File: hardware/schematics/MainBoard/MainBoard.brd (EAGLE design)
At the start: 85.1 x 107.6 mm, 16 parts, among them J1 T2M-105-01-X-D-TH-WT

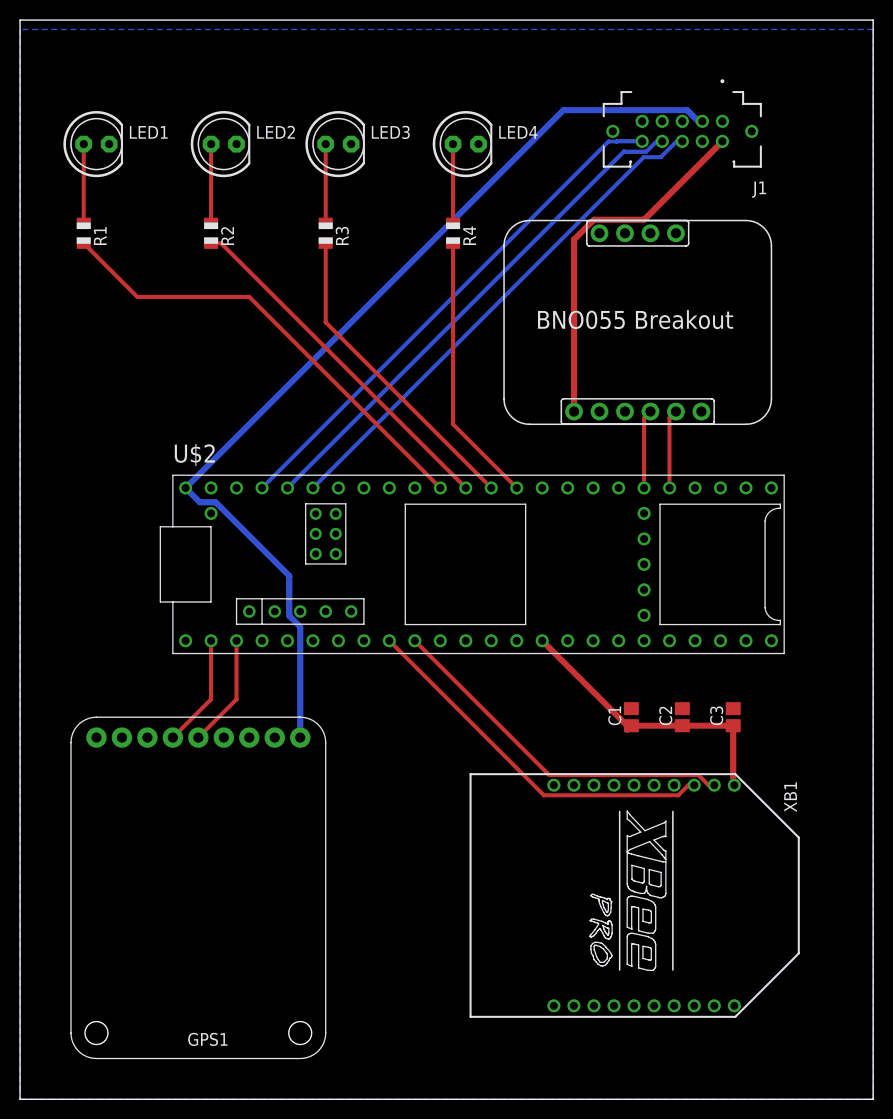
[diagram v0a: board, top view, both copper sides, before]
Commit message: Added BMP388 & PDF's
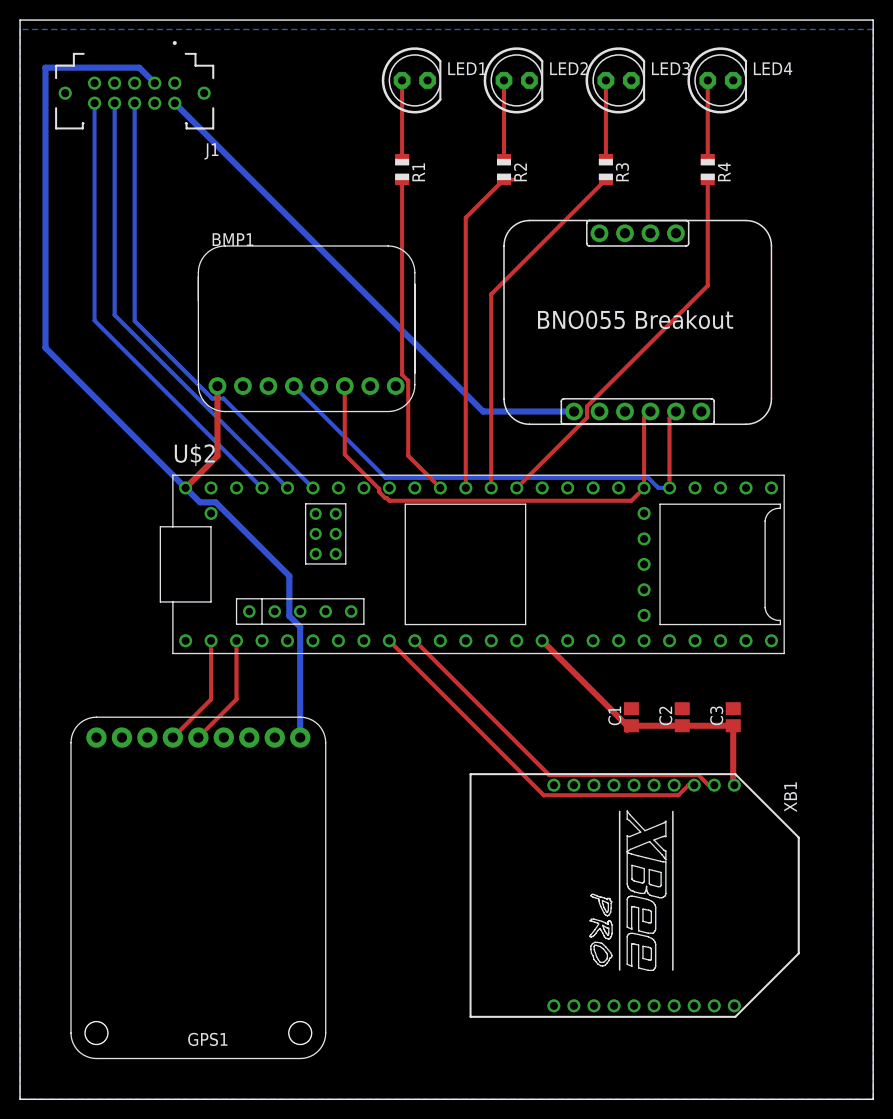
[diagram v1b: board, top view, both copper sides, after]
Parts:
- added BMP1: ADAFRUITBMP388, adafruit BMP388:ADAFRUITBMP388
- moved J1 54.7 mm to (11.4, 100.3)
- moved LED1 32.4 mm to (39.4, 101.6)
- moved R1 32.4 mm to (38.1, 92.7)
- moved LED2 29.9 mm to (49.5, 101.6)
- moved R2 29.9 mm to (48.3, 92.7)
- moved R3 28.7 mm to (58.4, 92.7)
- moved LED3 28.7 mm to (59.7, 101.6)
- moved R4 26.2 mm to (68.6, 92.7)
- moved LED4 26.2 mm to (69.8, 101.6)
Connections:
- net 3V3: now also BMP1.VIN
- net GND: now also BMP1.GND
- net SCL: now also BMP1.SCK
- net SDA: now also BMP1.SDI
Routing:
- net SCL: track 7.88 -> 49.6 mm
- net SDA: track 7.88 -> 47.2 mm
- net 5V: track 36.0 -> 52.6 mm
- net LED_1: track 45.7 -> 32.3 mm
- net LED_4: track 27.0 -> 38.6 mm
- net V_BATT: track 52.2 -> 45.3 mm
- net I_SENSE: track 51.7 -> 45.5 mm
- net BATT_TEMP: track 51.1 -> 46.4 mm
- net LED_3: track 31.2 -> 35.5 mm
- net 3V3: track 127.6 -> 130.7 mm
- net LED_2: track 35.5 -> 33.3 mm
